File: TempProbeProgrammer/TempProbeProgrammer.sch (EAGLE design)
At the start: 15 parts, among them U2 ATTINY841

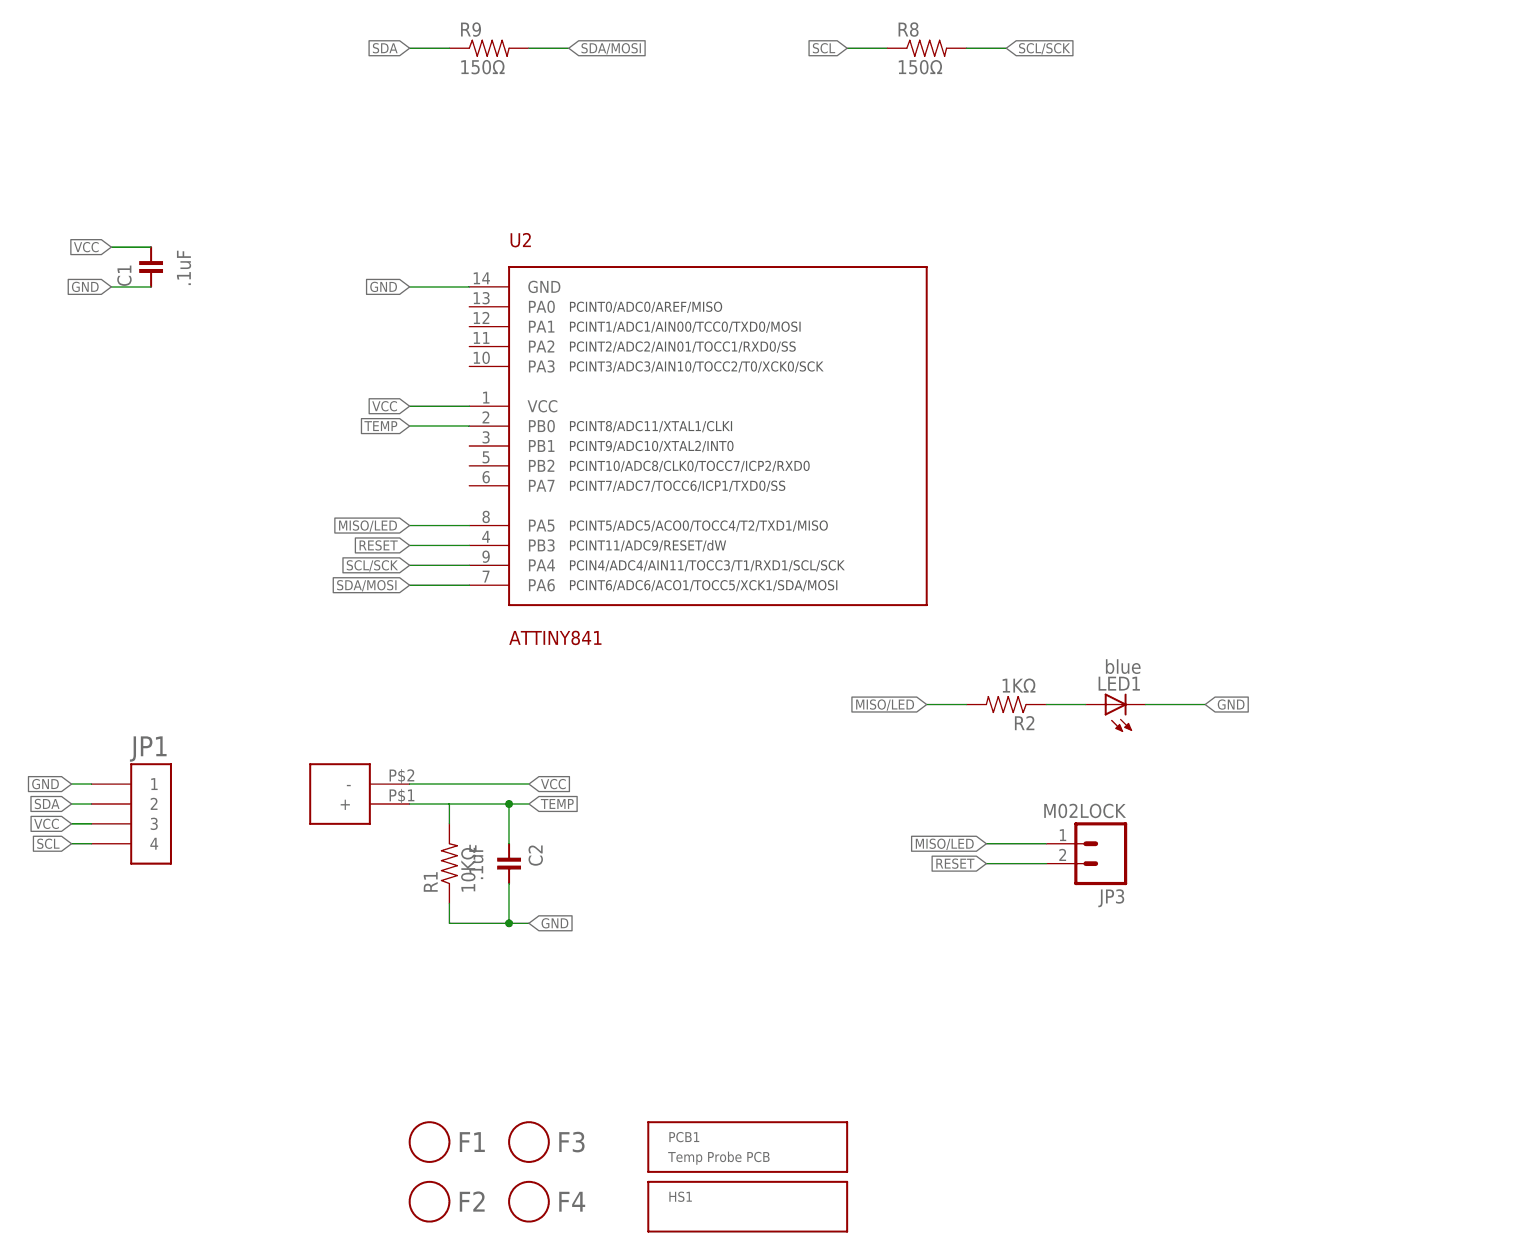
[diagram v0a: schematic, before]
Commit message: Revised temperature probe layout and created new temp probe programmer board
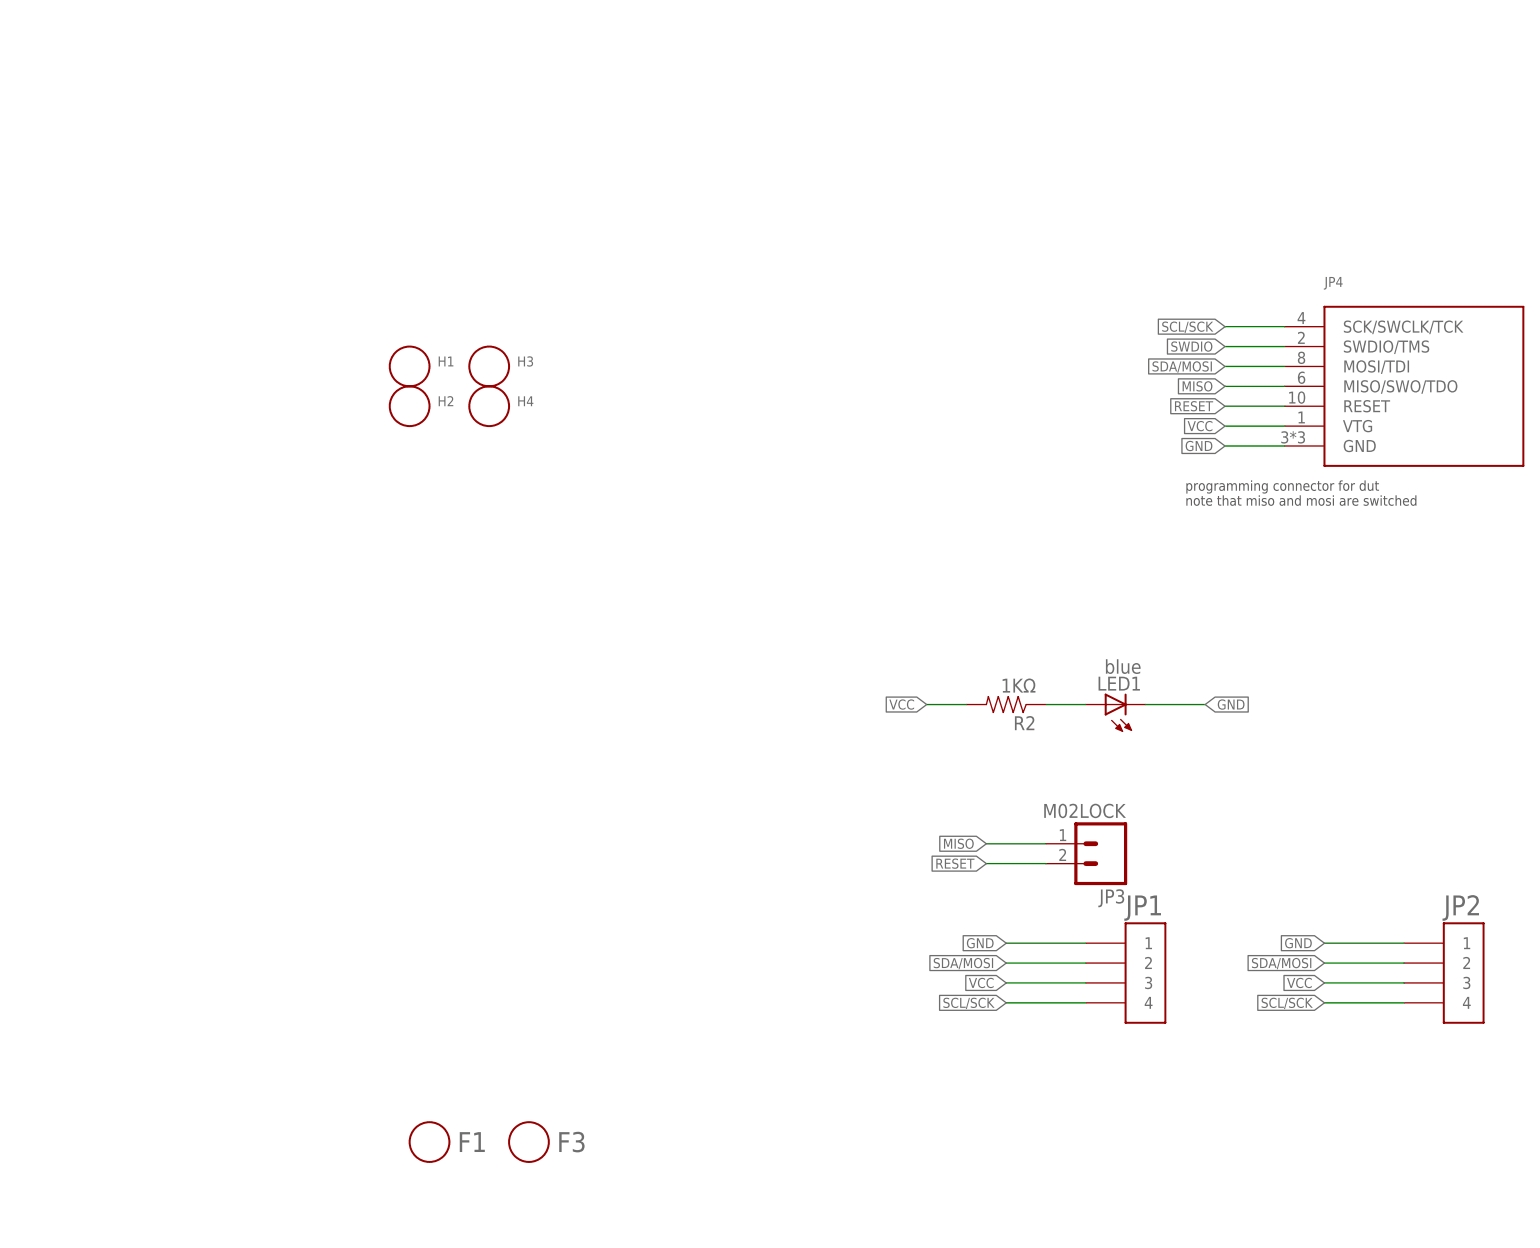
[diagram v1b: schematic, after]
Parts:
- removed C1, C2: .1uF, Modulo:CAPACITOR-.1UF
- removed F2, F4: FIDUCIAL, Modulo:FIDUCIAL
- removed PROBE1: TEMP-PROBE, Modulo:TEMP-PROBE
- removed R1: 10KΩ, Modulo:RESISTOR-10KΩ
- removed R8, R9: 150Ω, Modulo:RESISTOR-150Ω
- removed U2: ATTINY841, Modulo:ATTINY841
- added H1, H2, H3, H4: HOLE#4, Modulo:HOLE#4
- added JP2: HEADER-1X4-JST-PA-SIDE-SMD, Modulo:HEADER-1X4-JST-PA-SIDE-SMD
- added JP4: ICSP, Modulo:ICSP
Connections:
- removed net MISO/LED: JP3.1, R2.2, U2.PA5
- removed net SCL: JP1.4, R8.1
- removed net SDA: JP1.2, R9.1
- removed net TEMP: C2.2, PROBE1.+, R1.2, U2.PB0
- new net MISO: JP3.1, JP4.MISO/SWO/TDO
- new net SWDIO: JP4.SWDIO/TMS
- net GND: now also JP2.1, JP4.GND; no longer C1.2, C2.1, R1.1, U2.GND
- net RESET: now also JP4.RESET; no longer U2.PB3
- net SCL/SCK: now also JP1.4, JP2.4, JP4.SCK/SWCLK/TCK; no longer R8.2, U2.PA4
- net SDA/MOSI: now also JP1.2, JP2.2, JP4.MOSI/TDI; no longer R9.2, U2.PA6
- net VCC: now also JP2.3, JP4.VTG, R2.2; no longer C1.1, PROBE1.-, U2.VCC
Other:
- note added: "programming connector for dut note that miso and mosi are switched"
- moved on the sheet: JP1
